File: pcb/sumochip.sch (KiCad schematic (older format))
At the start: 53 parts, among them P1 CONN_01X05, P10 P10, P11 P11, P12 P12, P13 P13, P14 P14, P15 P15, P2 LED-toggle, P3 Power1, P4 Power2, P5 CONN_01X02, P6 P5, P7-8 CONN_02X05, Q1 OPTO_NPN, Q2 OPTO_NPN, Q3 OPTO_NPN, Q4 OPTO_NPN, Q5 OPTO_NPN, Q6 Q_NMOS_DGS

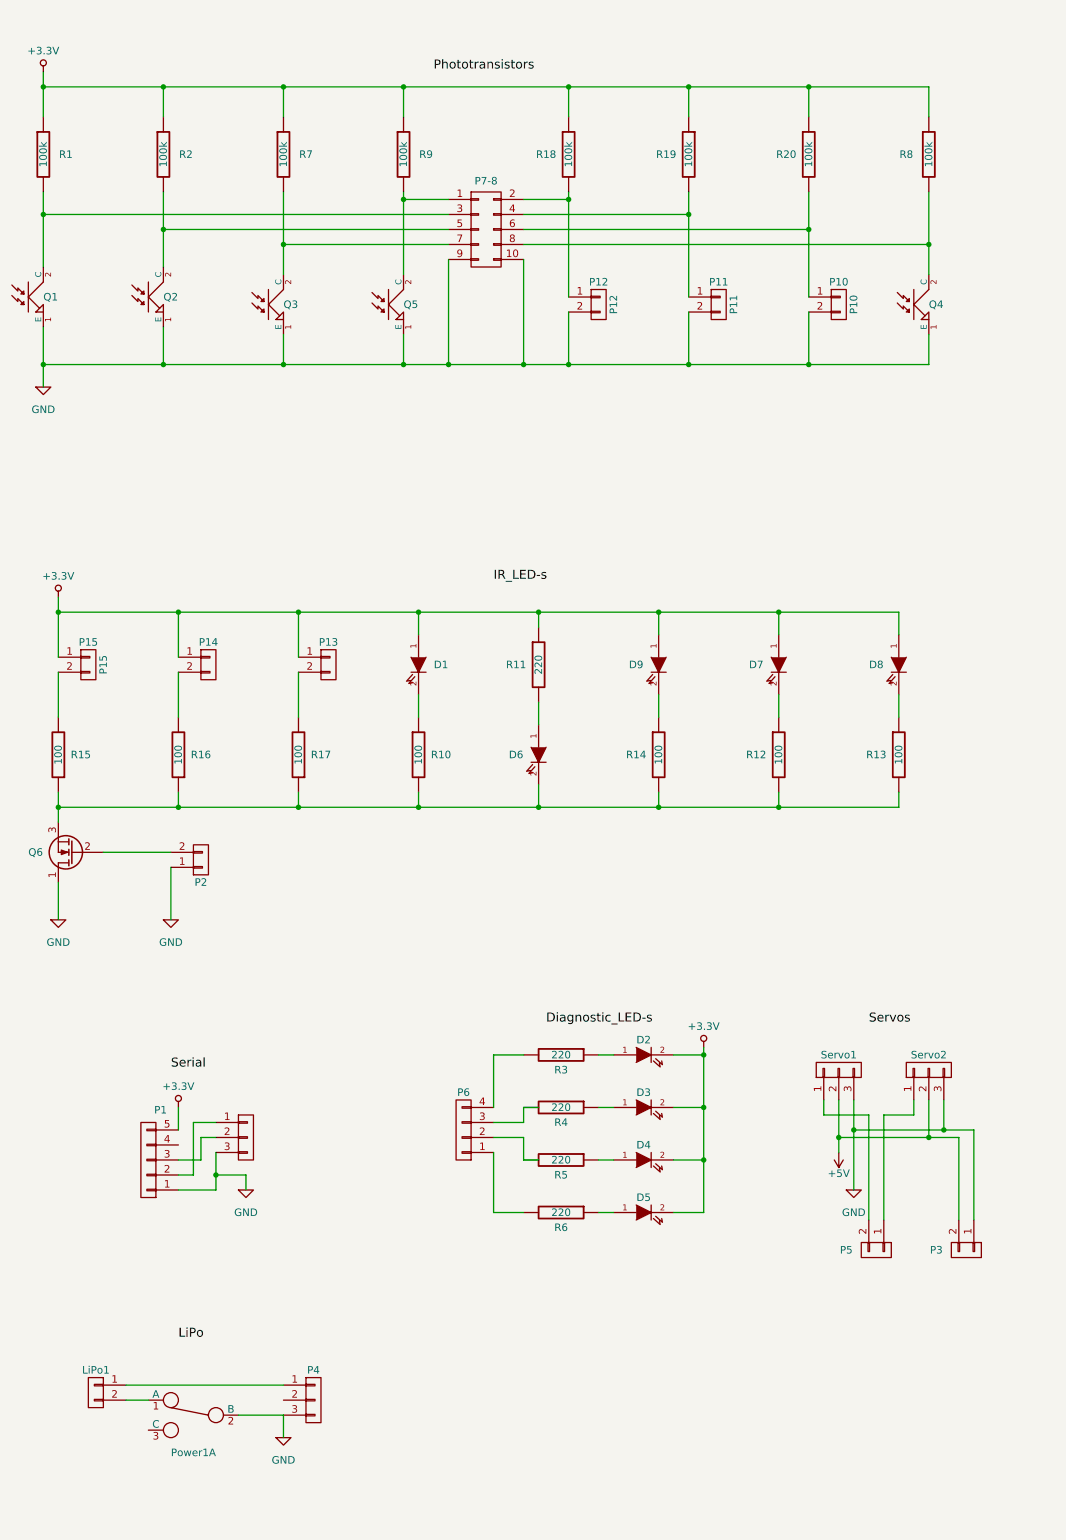
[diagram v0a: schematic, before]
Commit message: Add SumoCHIP PCB v1.1 schematic and layout
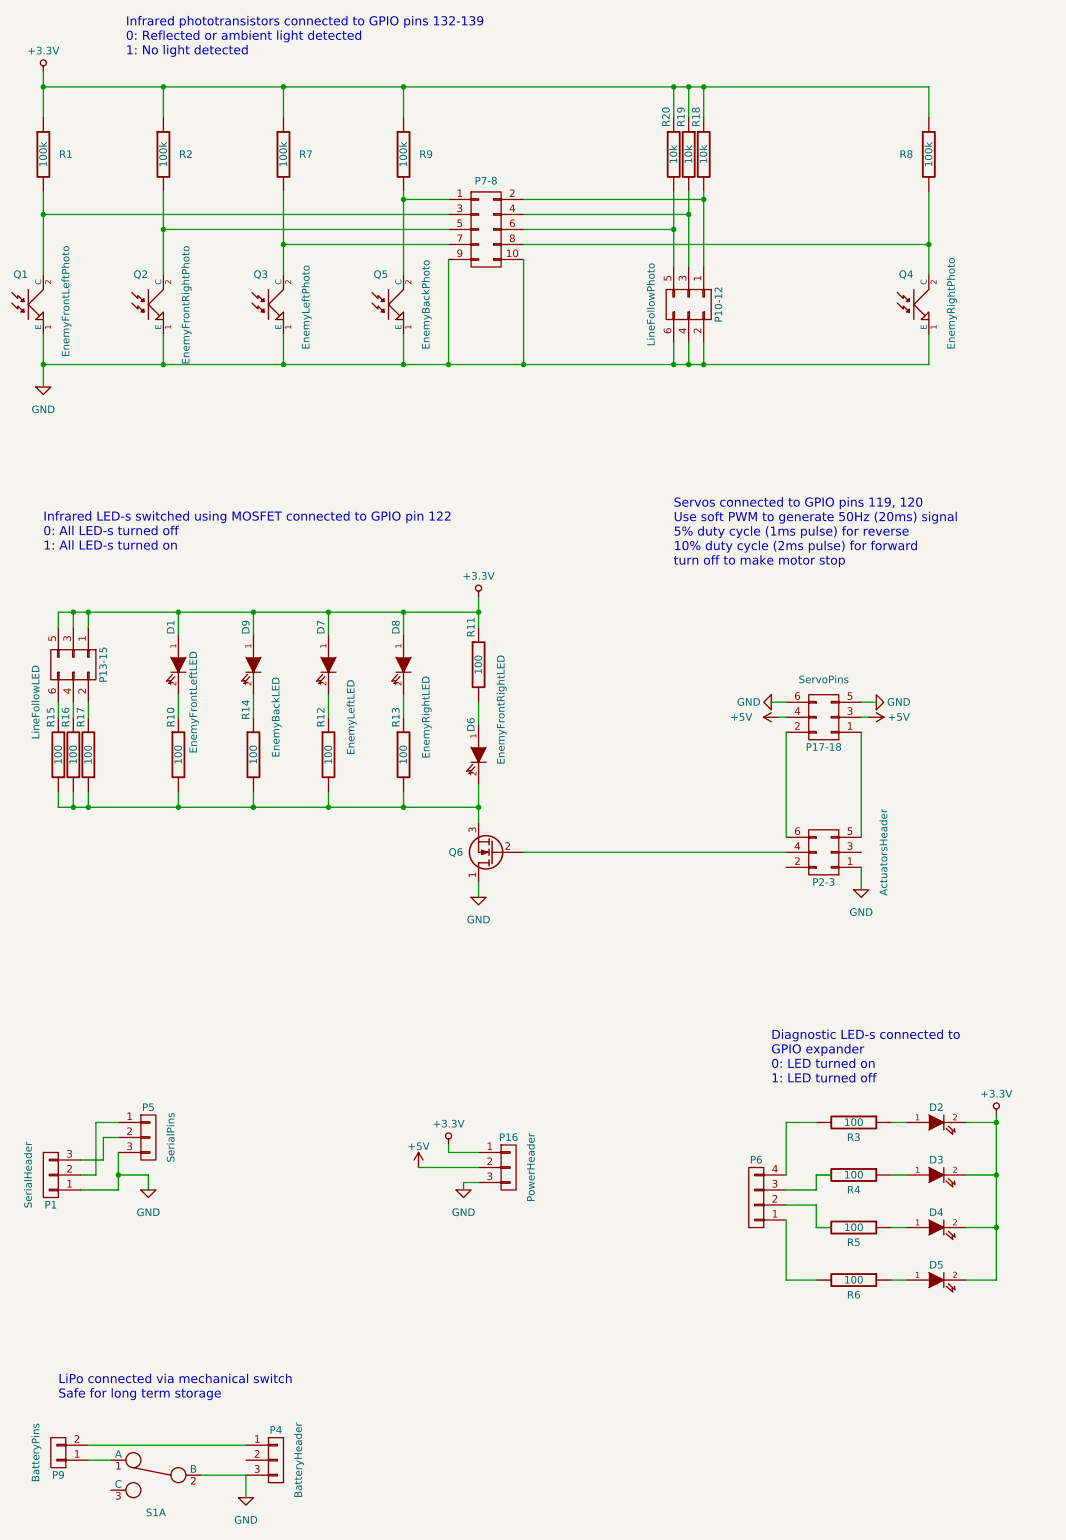
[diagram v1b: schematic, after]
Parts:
- removed P1: CONN_01X05, Pin_Headers:Pin_Header_Straight_1x05, symbol CONN_01X05
- removed P10: P10, Pin_Headers:Pin_Header_Straight_1x02, symbol CONN_01X02
- removed P11: P11, Pin_Headers:Pin_Header_Straight_1x02, symbol CONN_01X02
- removed P12: P12, Pin_Headers:Pin_Header_Straight_1x02, symbol CONN_01X02
- removed P13: P13, Pin_Headers:Pin_Header_Straight_1x02, symbol CONN_01X02
- removed P14: P14, Pin_Headers:Pin_Header_Straight_1x02, symbol CONN_01X02
- removed P15: P15, Pin_Headers:Pin_Header_Straight_1x02, symbol CONN_01X02
- removed P2: LED-toggle, Pin_Headers:Pin_Header_Straight_1x02, symbol CONN_01X02
- removed P3: Power1, Pin_Headers:Pin_Header_Straight_1x02, symbol CONN_01X02
- removed P5: CONN_01X02, Pin_Headers:Pin_Header_Straight_1x02, symbol CONN_01X02
- removed Servo1: Servo1, Pin_Headers:Pin_Header_Straight_1x03, symbol CONN_01X03
- removed Servo2: Servo2, Pin_Headers:Pin_Header_Straight_1x03, symbol CONN_01X03
- added P1: SerialHeader, Pin_Headers:Pin_Header_Straight_1x03, symbol CONN_01X03
- added P10-12: LineFollowPhoto, Pin_Headers:Pin_Header_Straight_2x03, symbol CONN_02X03
- added P13-15: LineFollowLED, Pin_Headers:Pin_Header_Straight_2x03, symbol CONN_02X03
- added P16: PowerHeader, Pin_Headers:Pin_Header_Straight_1x03, symbol CONN_01X03
- added P17-18: ServoPins, Pin_Headers:Pin_Header_Straight_2x03, symbol CONN_02X03
- added P2-3: ActuatorsHeader, Pin_Headers:Pin_Header_Straight_2x03, symbol CONN_02X03
- D1: value IR LED -> EnemyFrontLeftLED
- D6: value IR LED -> EnemyFrontRightLED
- D7: value IR LED -> EnemyLeftLED
- D8: value IR LED -> EnemyRightLED
- D9: value IR LED -> EnemyBackLED
- P4: value Power2 -> BatteryHeader
- P5: renamed from Serial1; value Serial -> SerialPins
- P6: value P5 -> DiagnosticHeader
- P7-8: value CONN_02X05 -> SensorsHeader
- P9: renamed from LiPo1; value 3.7V -> BatteryPins
- Q1: value OPTO_NPN -> EnemyFrontLeftPhoto
- Q2: value OPTO_NPN -> EnemyFrontRightPhoto
- Q3: value OPTO_NPN -> EnemyLeftPhoto
- Q4: value OPTO_NPN -> EnemyRightPhoto
- Q5: value OPTO_NPN -> EnemyBackPhoto
- Q6: value Q_NMOS_DGS -> 2N7000
- R11, R3, R4, R5, R6: value 220 -> 100
- R18, R19, R20: value 100k -> 10k
- renumbered Power1 to S1
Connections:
- net +3.3V: now also P13-15.1 (P1), P13-15.3 (P3), P13-15.5 (P5), P16.1 (P1)
- net +5V: now also P16.2 (P2), P17-18.3 (P3), P17-18.4 (P4)
- net GND: now also P1.1 (P1), P10-12.2 (P2), P10-12.4 (P4), P10-12.6 (P6), P16.3 (P3), P17-18.5 (P5), P17-18.6 (P6), P2-3.1 (P1)
- net at P4.1 (P1): now also P9.2 (P2); no longer P9.1 (P1)
- net at S1.1 (A): now also P9.1 (P1); no longer P9.2 (P2)
- net at P5.1 (P1): now also P1.2 (P2)
- net at P5.2 (P2): now also P1.3 (P3)
- net at Q6.2 (G): now also P2-3.4 (P4)
- net at R15.2: now also P13-15.6 (P6)
- net at R16.2: now also P13-15.4 (P4)
- net at R17.2: now also P13-15.2 (P2)
- net at P7-8.6 (P6), R20.2: now also P10-12.5 (P5)
- net at P7-8.4 (P4), R19.2: now also P10-12.3 (P3)
- net at P7-8.2 (P2), R18.2: now also P10-12.1 (P1)
- new net: P17-18.1 (P1), P2-3.5 (P5)
- new net: P17-18.2 (P2), P2-3.6 (P6)
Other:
- note added: "Diagnostic LED-s connected to\nGPIO expander\n0: LED turned on\n1: LED turned off"
- note added: "Infrared LED-s switched using MOSFET connected to GPIO pin 122\n0: All LED-s turned off\n1: All LED-s turned on\n"
- note added: "Infrared phototransistors connected to GPIO pins 132-139\n0: Reflected or ambient light detected\n1: No light detected"
- note added: "LiPo connected via mechanical switch\nSafe for long term storage"
- note added: "Servos connected to GPIO pins 119, 120\nUse soft PWM to generate 50Hz (20ms) signal\n5% duty cycle (1ms pulse) for reverse\n10% duty cycle (2ms pulse) for forward\nturn off to make motor stop"
- moved on the sheet: D1, D2, D3, D4, D5, D6, D7, D8, D9, P4, P6, P9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
